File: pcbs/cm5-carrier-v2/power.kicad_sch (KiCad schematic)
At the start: 0 parts

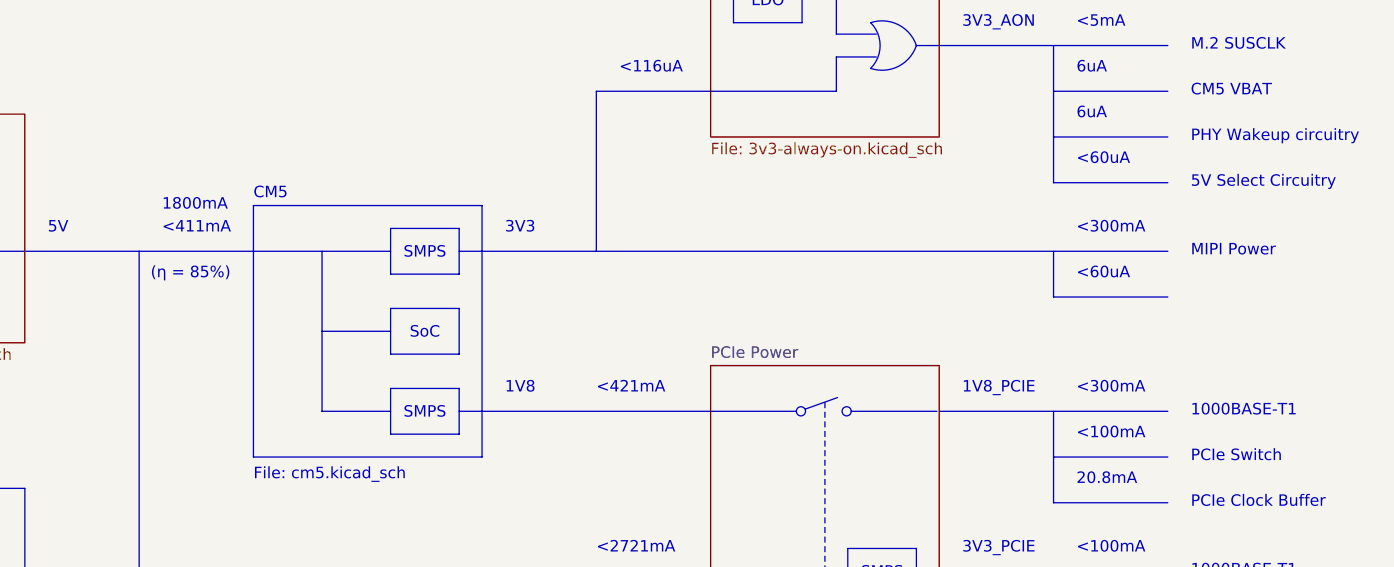
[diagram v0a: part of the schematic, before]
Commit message: Changed UART connector to I2C
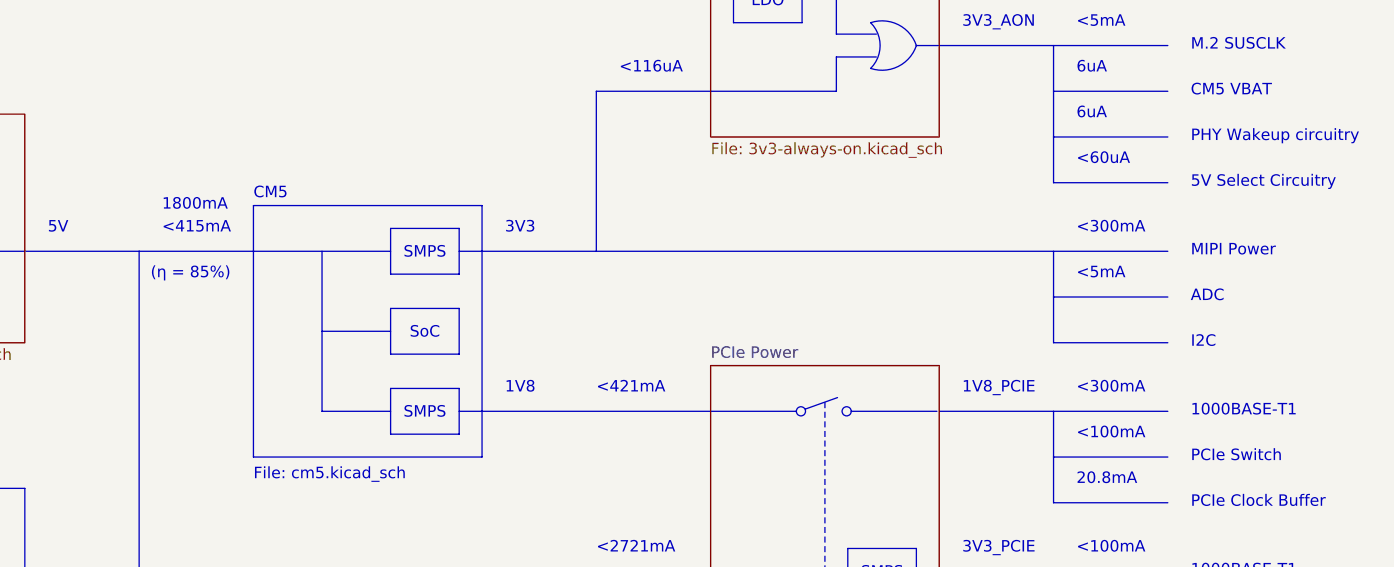
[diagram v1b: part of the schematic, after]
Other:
- note added: "<415mA"
- note added: "ADC"
- note added: "I2C"
- note removed: "<411mA"
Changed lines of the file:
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@@
 		)
 	)
-	(text "<411mA"
+	(text "<415mA"
 		(exclude_from_sim no)
 		(at 129.54 63.5 0)
@@
 		)
 	)
+	(text "I2C"
+		(exclude_from_sim no)
+		(at 243.84 76.2 0)
+		(effects
+			(font
+				(size 1.27 1.27)
+			)
+			(justify left)
+		)
+	)
 	(text "1V1"
 		(exclude_from_sim no)
@@
 		)
 	)
-	(text "<60uA"
+	(text "<5mA"
 		(exclude_from_sim no)
 		(at 231.14 68.58 0)
@@
 			)
 			(justify top)
+		)
+	)
+	(text "ADC"
+		(exclude_from_sim no)
+		(at 243.84 71.12 0)
+		(effects
+			(font
+				(size 1.27 1.27)
+			)
+			(justify left)
 		)
 	)
@@
 	(polyline
 		(pts
+			(xy 228.6 71.12) (xy 228.6 76.2)
+		)
+		(stroke
+			(width 0)
+			(type default)
+		)
+	)
+	(polyline
+		(pts
 			(xy 228.6 152.4) (xy 241.3 152.4)
 		)
@@
 		)
 		(stroke
+			(width 0)
+			(type default)
+		)
+	)
+	(polyline
+		(pts
+			(xy 241.3 76.2) (xy 228.6 76.2)
+		)
+		(stroke
